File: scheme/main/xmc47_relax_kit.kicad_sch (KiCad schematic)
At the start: 1 part

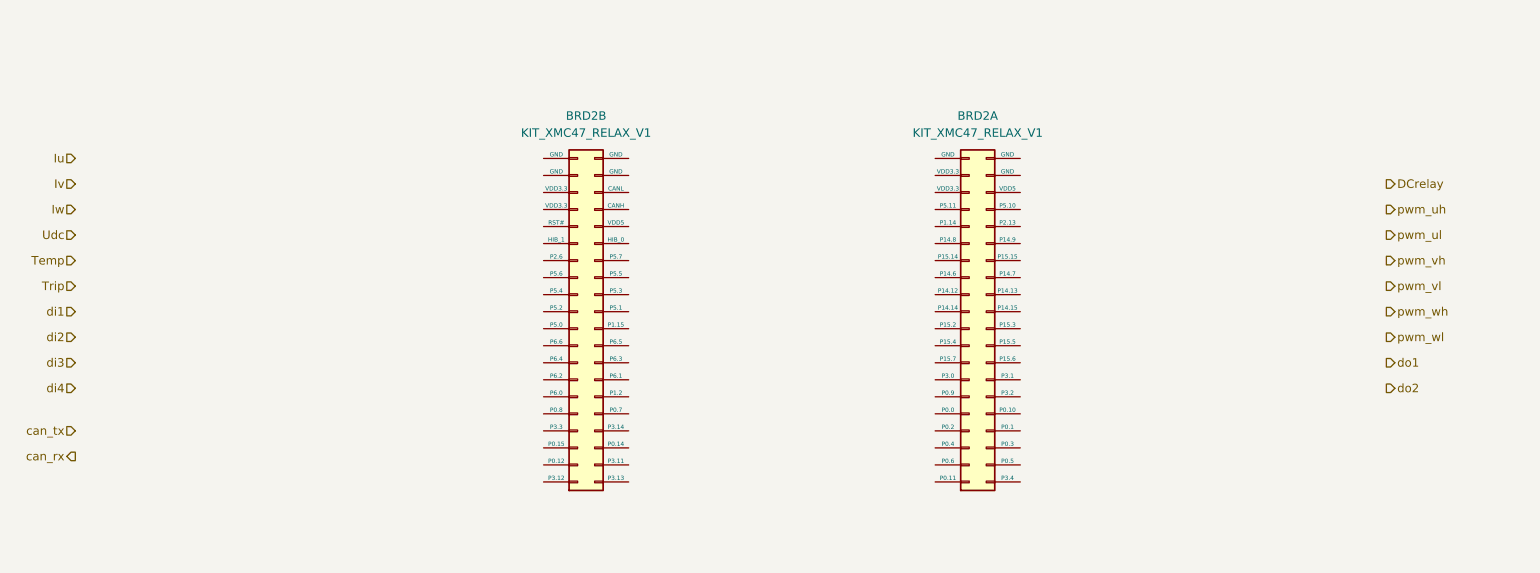
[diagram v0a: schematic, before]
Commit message: xmc47 relax kit connections
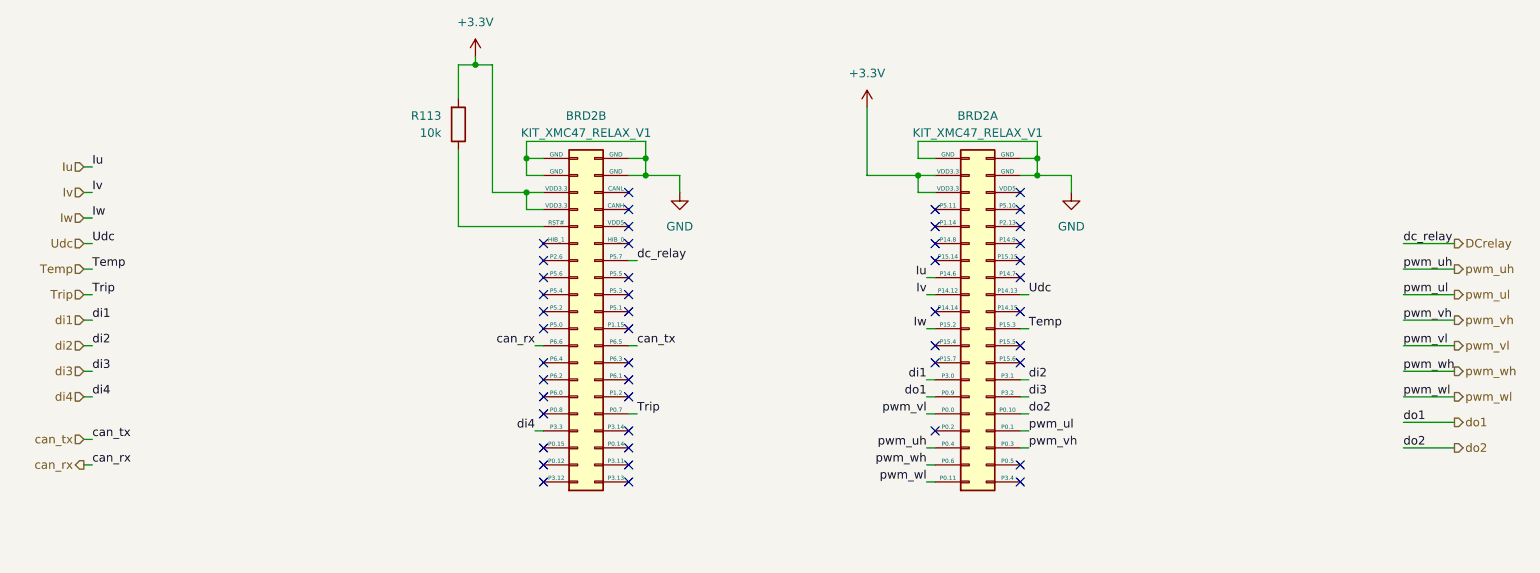
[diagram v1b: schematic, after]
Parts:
- added R113: 10k, Resistor_SMD:R_0805_2012Metric, symbol Device:R
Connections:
- net DCrelay: now also BRD2.27 (P5.7)
- net Iu: now also BRD2.26 (P14.6)
- net Iv: now also BRD2.24 (P14.12)
- net Iw: now also BRD2.20 (P15.2)
- net Temp: now also BRD2.19 (P15.3)
- net Trip: now also BRD2.9 (P0.7)
- net Udc: now also BRD2.23 (P14.13)
- net can_rx: now also BRD2.18 (P6.6)
- net can_tx: now also BRD2.17 (P6.5)
- net di1: now also BRD2.14 (P3.0)
- net di2: now also BRD2.13 (P3.1)
- net di3: now also BRD2.11 (P3.2)
- net di4: now also BRD2.8 (P3.3)
- net do1: now also BRD2.12 (P0.9)
- net do2: now also BRD2.9 (P0.10)
- net pwm_uh: now also BRD2.6 (P0.4)
- net pwm_ul: now also BRD2.7 (P0.1)
- net pwm_vh: now also BRD2.5 (P0.3)
- net pwm_vl: now also BRD2.10 (P0.0)
- net pwm_wh: now also BRD2.4 (P0.6)
- net pwm_wl: now also BRD2.2 (P0.11)
- net at BRD2.32 (RST#): now also R113.1
- net +3.3V: now reaches BRD2.34 (VDD3.3)
- net +3.3V: now also BRD2.36 (VDD3.3), BRD2.36 (VDD3.3), BRD2.38 (VDD3.3), R113.2
- net GND: now reaches BRD2.37 (GND)
- net GND: now also BRD2.37 (GND), BRD2.38 (GND), BRD2.39 (GND), BRD2.39 (GND), BRD2.40 (GND), BRD2.40 (GND)
- no-connect marks 0 -> 47

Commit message: added adc driver & output buffer with oe
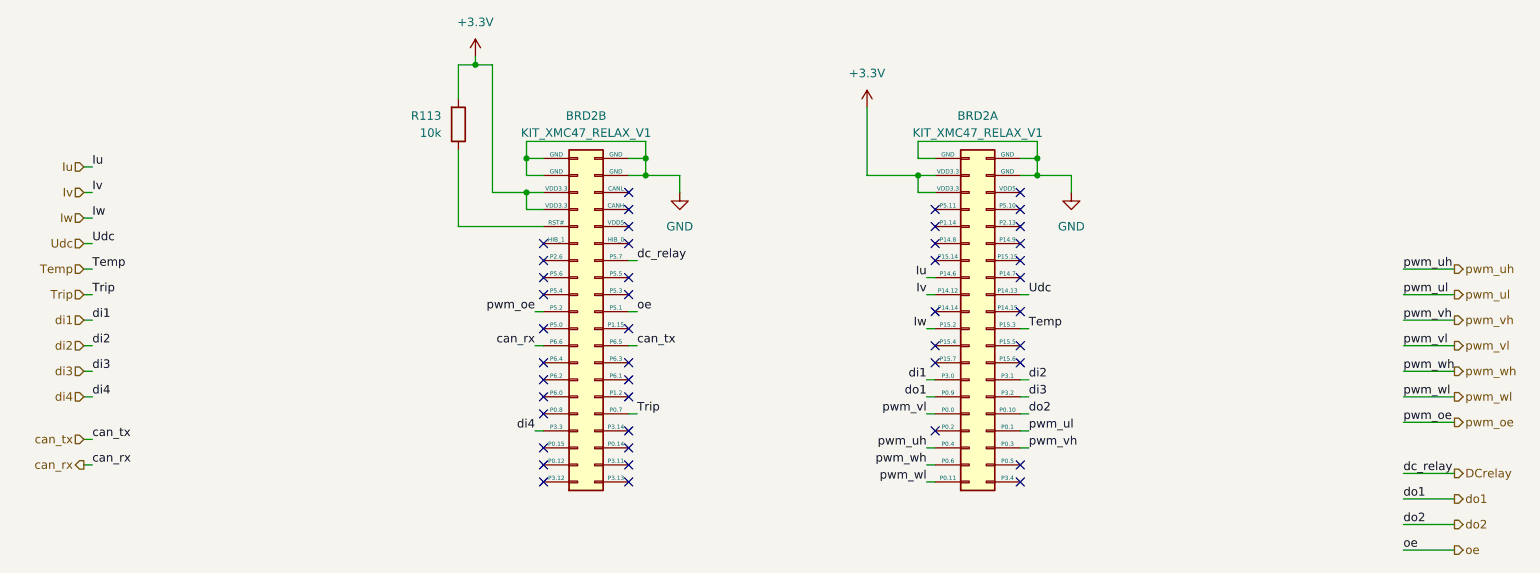
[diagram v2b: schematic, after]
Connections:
- net oe: now reaches BRD2.21 (P5.1)
- net pwm_oe: now reaches BRD2.22 (P5.2)
- no-connect marks 47 -> 45
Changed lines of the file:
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@@
-	)
-	(no_connect
-		(at 129.54 69.85)
 	)
 	(no_connect
@@
 	)
 	(no_connect
-		(at 116.84 69.85)
-	)
-	(no_connect
 		(at 129.54 52.07)
 	)
@@
 	(wire
 		(pts
+			(xy 245.11 86.36) (xy 252.73 86.36)
+		)
+		(stroke
+			(width 0)
+			(type default)
+		)
+	)
+	(wire
+		(pts
 			(xy 116.84 57.15) (xy 104.14 57.15)
 		)
@@
 	(wire
 		(pts
-			(xy 245.11 86.36) (xy 252.73 86.36)
+			(xy 245.11 97.79) (xy 252.73 97.79)
 		)
 		(stroke
@@
 	(wire
 		(pts
+			(xy 245.11 105.41) (xy 252.73 105.41)
+		)
+		(stroke
+			(width 0)
+			(type default)
+		)
+	)
+	(wire
+		(pts
 			(xy 114.3 54.61) (xy 114.3 52.07)
 		)
@@
 	(wire
 		(pts
+			(xy 115.57 69.85) (xy 116.84 69.85)
+		)
+		(stroke
+			(width 0)
+			(type default)
+		)
+	)
+	(wire
+		(pts
 			(xy 190.5 44.45) (xy 190.5 46.99)
 		)
@@
 	(wire
 		(pts
-			(xy 245.11 59.69) (xy 252.73 59.69)
+			(xy 245.11 93.98) (xy 252.73 93.98)
 		)
 		(stroke
@@
 	(wire
 		(pts
+			(xy 129.54 69.85) (xy 130.81 69.85)
+		)
+		(stroke
+			(width 0)
+			(type default)
+		)
+	)
+	(wire
+		(pts
 			(xy 173.99 90.17) (xy 175.26 90.17)
 		)
@@
 	(wire
 		(pts
-			(xy 245.11 90.17) (xy 252.73 90.17)
+			(xy 245.11 101.6) (xy 252.73 101.6)
 		)
 		(stroke
@@
 	)
 	(label "dc_relay"
-		(at 245.11 59.69 0)
+		(at 245.11 93.98 0)
+		(effects
+			(font
+				(size 1.27 1.27)
+			)
+			(justify left bottom)
+		)
+	)
+	(label "oe"
+		(at 130.81 69.85 0)
 		(effects
 			(font
@@
 	)
 	(label "do2"
-		(at 245.11 90.17 0)
+		(at 245.11 101.6 0)
+		(effects
+			(font
+				(size 1.27 1.27)
+			)
+			(justify left bottom)
+		)
+	)
+	(label "pwm_oe"
+		(at 245.11 86.36 0)
 		(effects
 			(font
@@
 	)
 	(label "do1"
-		(at 245.11 86.36 0)
-		(effects
-			(font
-				(size 1.27 1.27)
-			)
-			(justify left bottom)
+		(at 245.11 97.79 0)
+		(effects
+			(font
+				(size 1.27 1.27)
+			)
+			(justify left bottom)
+		)
+	)
+	(label "pwm_oe"
+		(at 115.57 69.85 180)
+		(effects
+			(font
+				(size 1.27 1.27)
+			)
+			(justify right bottom)
 		)
 	)
@@
 			)
 			(justify right bottom)
+		)
+	)
+	(label "oe"
+		(at 245.11 105.41 0)
+		(effects
+			(font
+				(size 1.27 1.27)
+			)
+			(justify left bottom)
 		)
 	)
@@
 	(hierarchical_label "do1"
 		(shape output)
-		(at 252.73 86.36 0)
+		(at 252.73 97.79 0)
+		(effects
+			(font
+				(size 1.27 1.27)
+			)
+			(justify left)
+		)
+	)
+	(hierarchical_label "oe"
+		(shape output)
+		(at 252.73 105.41 0)
 		(effects
 			(font
@@
 	(hierarchical_label "do2"
 		(shape output)
-		(at 252.73 90.17 0)
+		(at 252.73 101.6 0)
 		(effects
 			(font
@@
 	(hierarchical_label "DCrelay"
 		(shape output)
-		(at 252.73 59.69 0)
+		(at 252.73 93.98 0)
 		(effects
 			(font
@@
 		)
 	)
+	(hierarchical_label "pwm_oe"
+		(shape output)
+		(at 252.73 86.36 0)
+		(effects
+			(font
+				(size 1.27 1.27)
+			)
+			(justify left)
+		)
+	)

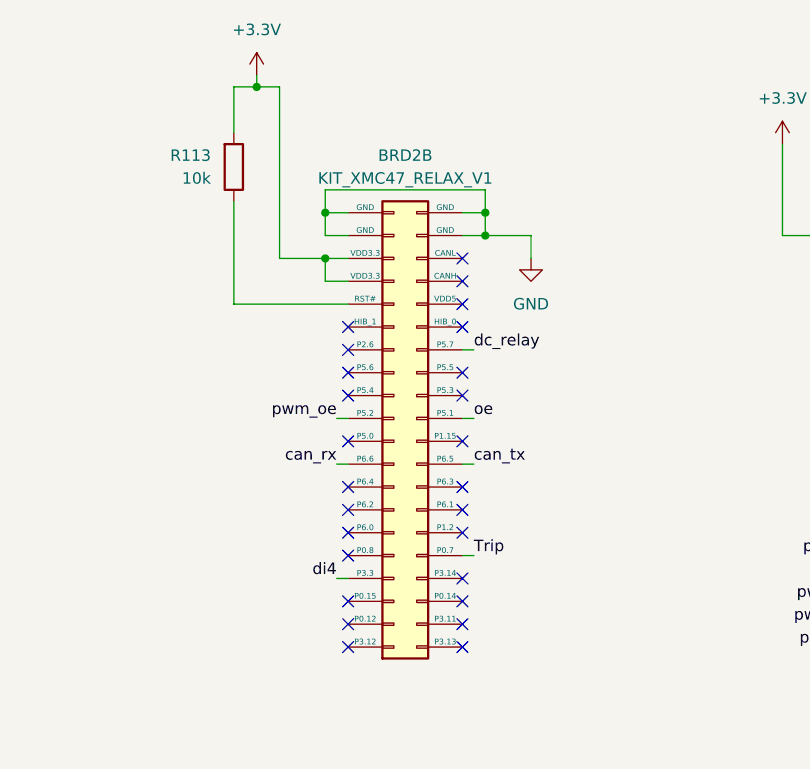
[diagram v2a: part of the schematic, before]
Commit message: control boards symbols & footprints updated
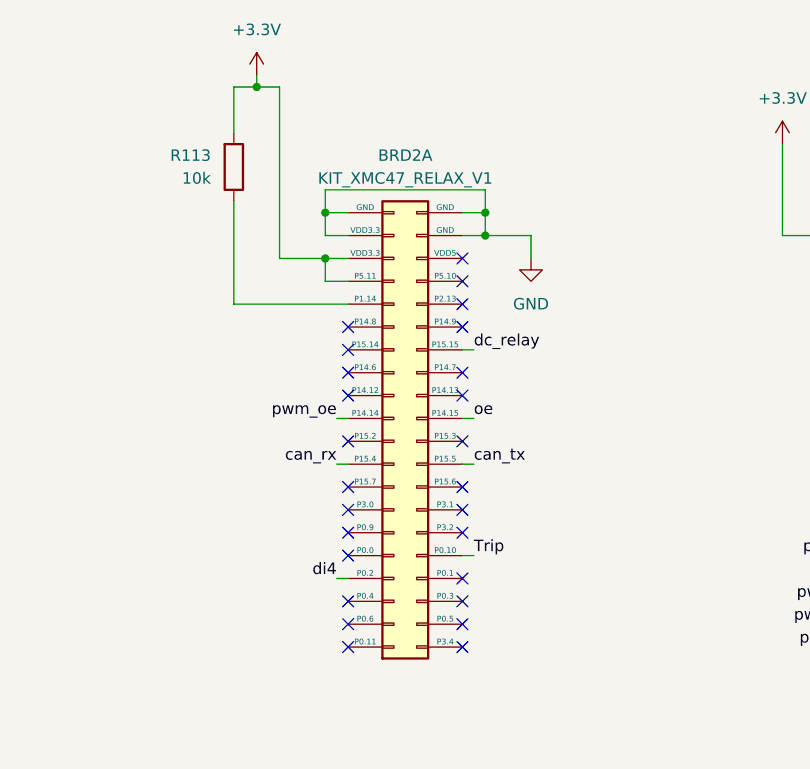
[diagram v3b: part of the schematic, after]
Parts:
- BRD2: footprint (none) -> main:XMC47_RELAX_KIT_V1
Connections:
- net +3.3V: now also BRD2.X1_34 (P5.11), BRD2.X1_36 (VDD3.3), BRD2.X1_36 (VDD3.3), BRD2.X1_38 (VDD3.3); no longer BRD2.34 (VDD3.3), BRD2.36 (VDD3.3), BRD2.36 (VDD3.3), BRD2.38 (VDD3.3)
- net DCrelay: now also BRD2.X1_27 (P15.15); no longer BRD2.27 (P5.7)
- net GND: now also BRD2.X1_37 (GND), BRD2.X1_37 (GND), BRD2.X1_38 (VDD3.3), BRD2.X1_39 (GND), BRD2.X1_39 (GND), BRD2.X1_40 (GND), BRD2.X1_40 (GND); no longer BRD2.37 (GND), BRD2.37 (GND), BRD2.38 (GND), BRD2.39 (GND), BRD2.39 (GND), BRD2.40 (GND), BRD2.40 (GND)
- net Iu: now also BRD2.X1_26 (P14.6); no longer BRD2.26 (P14.6)
- net Iv: now also BRD2.X1_24 (P14.12); no longer BRD2.24 (P14.12)
- net Iw: now also BRD2.X1_20 (P15.2); no longer BRD2.20 (P15.2)
- net Temp: now also BRD2.X1_19 (P15.3); no longer BRD2.19 (P15.3)
- net Trip: now also BRD2.X1_9 (P0.10); no longer BRD2.9 (P0.7)
- net Udc: now also BRD2.X1_23 (P14.13); no longer BRD2.23 (P14.13)
- net can_rx: now also BRD2.X1_18 (P15.4); no longer BRD2.18 (P6.6)
- net can_tx: now also BRD2.X1_17 (P15.5); no longer BRD2.17 (P6.5)
- net di1: now also BRD2.X1_14 (P3.0); no longer BRD2.14 (P3.0)
- net di2: now also BRD2.X1_13 (P3.1); no longer BRD2.13 (P3.1)
- net di3: now also BRD2.X1_11 (P3.2); no longer BRD2.11 (P3.2)
- net di4: now also BRD2.X1_8 (P0.2); no longer BRD2.8 (P3.3)
- net do1: now also BRD2.X1_12 (P0.9); no longer BRD2.12 (P0.9)
- net do2: now also BRD2.X1_9 (P0.10); no longer BRD2.9 (P0.10)
- net oe: now also BRD2.X1_21 (P14.15); no longer BRD2.21 (P5.1)
- net pwm_oe: now also BRD2.X1_22 (P14.14); no longer BRD2.22 (P5.2)
- net pwm_uh: now also BRD2.X1_6 (P0.4); no longer BRD2.6 (P0.4)
- net pwm_ul: now also BRD2.X1_7 (P0.1); no longer BRD2.7 (P0.1)
- net pwm_vh: now also BRD2.X1_5 (P0.3); no longer BRD2.5 (P0.3)
- net pwm_vl: now also BRD2.X1_10 (P0.0); no longer BRD2.10 (P0.0)
- net pwm_wh: now also BRD2.X1_4 (P0.6); no longer BRD2.4 (P0.6)
- net pwm_wl: now also BRD2.X1_2 (P0.11); no longer BRD2.2 (P0.11)
- net at R113.1: now also BRD2.X1_32 (P1.14); no longer BRD2.32 (RST#)

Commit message: sheets titles
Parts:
- BRD2: footprint (none) -> main:XMC47_RELAX_KIT_V1
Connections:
- net +3.3V: now also BRD2.X2_34 (VDD3.3), BRD2.X2_36 (VDD3.3); no longer BRD2.X1_34 (P5.11), BRD2.X1_36 (VDD3.3)
- net DCrelay: now also BRD2.X2_27 (P5.7); no longer BRD2.X1_27 (P15.15)
- net GND: now also BRD2.X2_37 (GND), BRD2.X2_38 (GND), BRD2.X2_39 (GND), BRD2.X2_40 (GND); no longer BRD2.X1_37 (GND), BRD2.X1_38 (VDD3.3), BRD2.X1_39 (GND), BRD2.X1_40 (GND)
- net Trip: now also BRD2.X2_9 (P0.7); no longer BRD2.X1_9 (P0.10)
- net can_rx: now also BRD2.X2_18 (P6.6); no longer BRD2.X1_18 (P15.4)
- net can_tx: now also BRD2.X2_17 (P6.5); no longer BRD2.X1_17 (P15.5)
- net di4: now also BRD2.X2_8 (P3.3); no longer BRD2.X1_8 (P0.2)
- net oe: now also BRD2.X2_21 (P5.1); no longer BRD2.X1_21 (P14.15)
- net pwm_oe: now also BRD2.X2_22 (P5.2); no longer BRD2.X1_22 (P14.14)
- net at R113.1: now also BRD2.X2_32 (RST#); no longer BRD2.X1_32 (P1.14)
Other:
- title: (none) -> Плата KIT_XMC47_RELAX_V1
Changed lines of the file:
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@@
 	(generator_version "8.0")
 	(paper "A4")
+	(title_block
+		(title "Плата KIT_XMC47_RELAX_V1")
+	)
 	(junction
 		(at 190.5 46.99)
@@
 		(lib_id "main:KIT_XMC47_RELAX_V1")
 		(at 123.19 69.85 0)
-		(unit 1)
+		(unit 2)
 		(exclude_from_sim no)
 		(in_bom yes)
@@
 				(path "/c11d1dbc-4db9-4712-8d1d-5f6f7086cded/e3db07b5-d47c-4d55-bf51-a423335924fb/037f9fd3-aec8-42fc-8807-97ab6f40e6e8"
 					(reference "BRD2")
-					(unit 1)
+					(unit 2)
 				)
 			)
@@
 			)
 		)
-		(property "Footprint" ""
+		(property "Footprint" "main:XMC47_RELAX_KIT_V1"
 			(at 181.61 69.85 0)
 			(effects

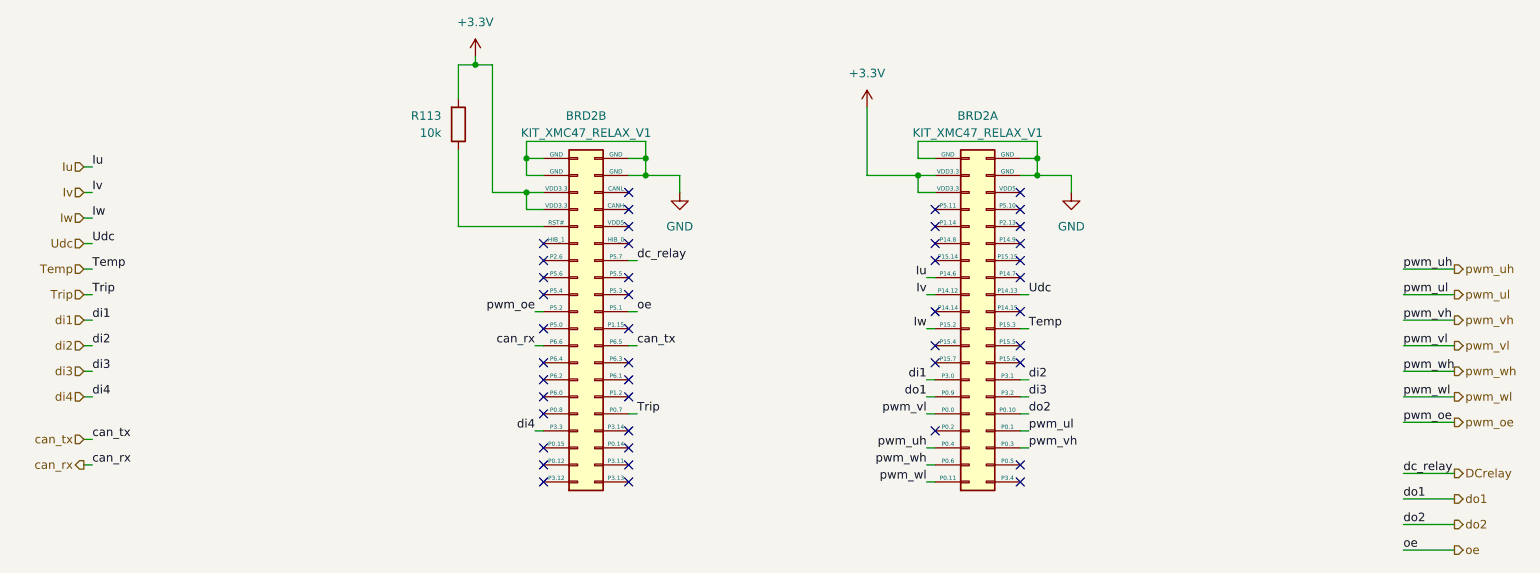
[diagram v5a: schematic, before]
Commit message: added analog input 0 && sheets sort
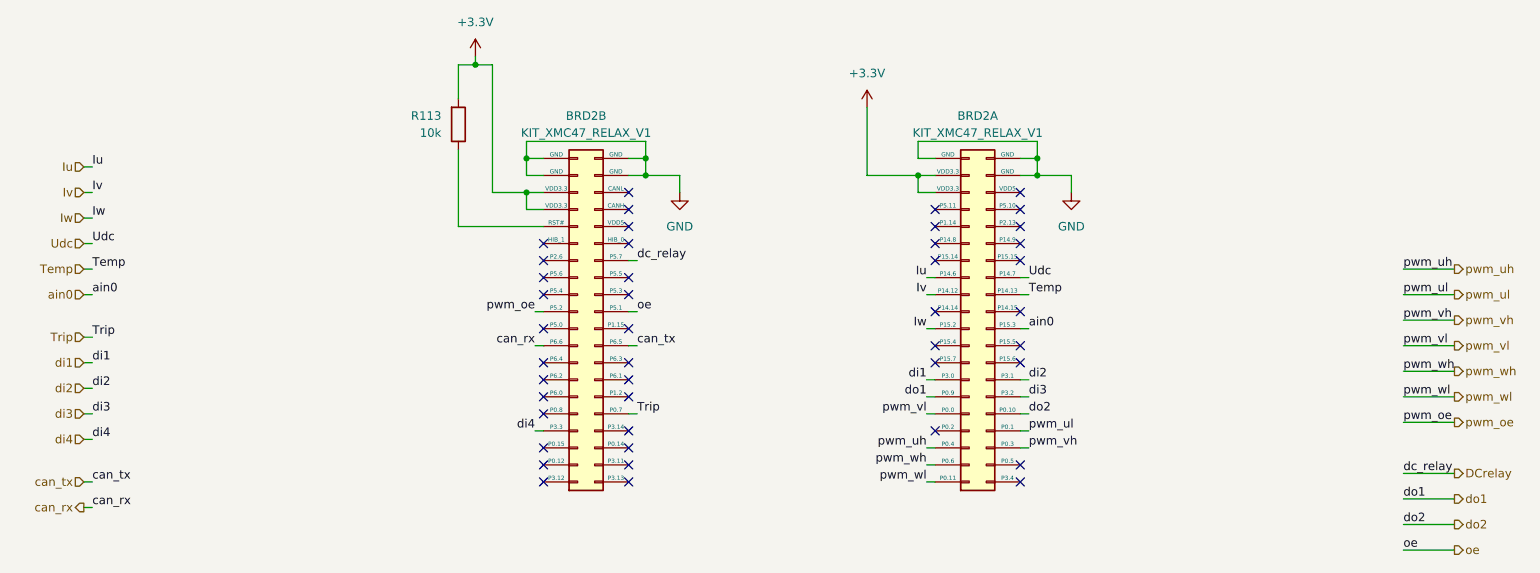
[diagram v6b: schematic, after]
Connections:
- net Temp: now also BRD2.X1_23 (P14.13); no longer BRD2.X1_19 (P15.3)
- net Udc: now also BRD2.X1_25 (P14.7); no longer BRD2.X1_23 (P14.13)
- new net ain0: BRD2.X1_19 (P15.3)
- no-connect marks 45 -> 44
